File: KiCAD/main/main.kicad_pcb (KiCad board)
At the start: 2 copper layers, 46 parts, among them J1 USB_C_Receptacle_USB2.0_14P, J2 Conn_Coaxial, SW1 SW_SPDT, SW2 SW_Push, SW3 SW_Push, U1 SX1262IMLTRT, U2 TP4056-42-ESOP8, U3 TLV75533PDRV, U4 ESP32-S3-MINI-1, U5 BGS12WN6E6327, U7 CH340X

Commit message: rev 2!
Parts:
- removed D3, D4, D5: LED, LED_SMD:LED_0402_1005Metric
- removed R12: 1K, Resistor_SMD:R_01005_0402Metric
- removed R3, R8: 10K, Resistor_SMD:R_01005_0402Metric
- removed R6: 2K, Resistor_SMD:R_01005_0402Metric
- removed SW2: SW_Push, Button_Switch_SMD:SW_SPST_PTS810
- removed SW3: SW_Push, Button_Switch_SMD:SW_SPST_PTS645Sx43SMTR92
- removed U5: BGS12WN6E6327, Package_LGA:Infineon_PG-TSNP-6-10_0.7x1.1mm_0.7x1.1mm_P0.4mm
- added C5: 470pF, Capacitor_SMD:C_0603_1608Metric, F.Cu at (101.4, 78.9)
- added R10: 10K, Resistor_SMD:R_0603_1608Metric, F.Cu at (93.1, 48.9)
- added R9: 10K, Resistor_SMD:R_0603_1608Metric, F.Cu at (93.1, 45.4)
- added U6: MIC5219-3.3YMM, Package_SO:MSOP-8_3x3mm_P0.65mm, F.Cu at (97.2, 77.7)
- C1, C12, C14, C15, C16, C2: footprint Capacitor_SMD:C_01005_0402Metric -> Capacitor_SMD:C_0603_1608Metric
- C10, C11, C13, C17, C18, C3, C6, C7: footprint Capacitor_SMD:C_01005_0402Metric -> Capacitor_SMD:C_0402_1005Metric
- C4: footprint Capacitor_SMD:C_01005_0402Metric -> Capacitor_SMD:C_0805_2012Metric
- D1, D2: footprint Diode_SMD:D_01005_0402Metric -> Diode_SMD:D_SOD-323
- FL1: value 0900FM15K0039001E -> 0900FM15K0039; footprint customlib:0900FM15K0039001E_JOT-L -> RF_Converter:Balun_Johanson_0900FM15K0039
- G***: moved to B.Cu
- L1: footprint Inductor_SMD:L_01005_0402Metric -> Inductor_SMD:L_0805_2012Metric
- L2: footprint Inductor_SMD:L_01005_0402Metric -> Inductor_SMD:L_0603_1608Metric
- R1, R2, R4, R7: footprint Resistor_SMD:R_01005_0402Metric -> Resistor_SMD:R_0603_1608Metric
- R5: footprint Resistor_SMD:R_01005_0402Metric -> Resistor_SMD:R_0402_1005Metric
- SW1: footprint Button_Switch_SMD:SW_SPDT_PCM12 -> customlib:SSSS810701
- U3: value TLV75533PDRV -> BGS12P2L; footprint Package_SON:WSON-6-1EP_2x2mm_P0.65mm_EP1x1.6mm -> Package_LGA:Infineon_PG-TSNP-6-10_0.7x1.1mm_0.7x1.1mm_P0.4mm
- moved J2 142.7 mm to (100.3, 32.9), turned to 90 degrees
- moved G*** 100.0 mm to (105.5, 87.0), turned to 180 degrees
- moved C14 92.1 mm to (99.2, 40.1), turned to -135 degrees
- moved R4 67.2 mm to (97.1, 49.6), turned to 0 degrees
- moved C10 66.7 mm to (94.6, 47.5)
- moved C7 65.5 mm to (94.6, 45.0), turned to 90 degrees
- moved C1 63.1 mm to (94.8, 81.8)
- moved U1 62.6 mm to (98.8, 46.0), turned to -90 degrees
- moved D1 62.2 mm to (97.5, 84.0), turned to -90 degrees
- moved C11 62.0 mm to (95.6, 42.9), turned to 90 degrees
- moved L1 61.7 mm to (95.7, 41.0), turned to 180 degrees
- moved C16 61.2 mm to (91.8, 75.8)
- moved SW1 60.9 mm to (91.7, 82.5), turned to -90 degrees
- moved C15 60.9 mm to (101.0, 84.9), turned to 0 degrees
- moved C6 60.4 mm to (97.2, 42.4), turned to 180 degrees
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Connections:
- net CHRG renamed CHRG_BAT
- C13 pad 1: Net-(U5-CTRL) -> Net-(U3-CTRL)
- J1 pad A8: (no net) -> USB_DATA-
- R5 pad 2: Net-(U5-CTRL) -> Net-(U3-CTRL)
- U2 pad 6: Net-(D3-K) -> ~{STDBY}
- U2 pad 7: Net-(D4-K) -> ~{CHRG}
- U3 pad 1: VCC -> Net-(FL1-SW_RFO)
- U3 pad 2: unconnected-(U3-NC-Pad2) -> V-
- U3 pad 3: V- -> Net-(FL1-SW_RFI)
- U3 pad 4: Net-(SW1-A) -> VCC
- U3 pad 5: unconnected-(U3-NC-Pad5) -> Net-(J2-In)
- U3 pad 6: Net-(SW1-A) -> Net-(U3-CTRL)
- U4 pad 10: SPI_CLK -> SPI_MOSI
- U4 pad 11: SPI_MOSI -> READY
- U4 pad 12: SPI_MISO -> unconnected-(U4-IO8-Pad12)
- U4 pad 13: READY -> unconnected-(U4-IO9-Pad13)
- U4 pad 14: Net-(U4-IO10) -> unconnected-(U4-IO10-Pad14)
- U4 pad 20: unconnected-(U4-IO16-Pad20) -> ~{CHRG}
- U4 pad 21: unconnected-(U4-IO17-Pad21) -> ~{STDBY}
- U4 pad 29: unconnected-(U4-IO34-Pad29) -> IO34
- U4 pad 31: Net-(U4-IO35) -> IO35
- U4 pad 32: Net-(D5-K) -> IO36
- U4 pad 45: Net-(U4-EN) -> unconnected-(U4-EN-Pad45)
- U4 pad 7: unconnected-(U4-IO3-Pad7) -> SPI_CS
- U4 pad 8: unconnected-(U4-IO4-Pad8) -> SPI_CLK
- U4 pad 9: SPI_CS -> SPI_MISO
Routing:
- net V-: track 178.9 -> 259.0 mm, vias 9 -> 15
- net VCC: track 51.1 -> 108.9 mm, vias 2 -> 4
- net ~{STDBY}: track 0.00 -> 34.4 mm, vias 0 -> 2
- net ~{CHRG}: track 0.00 -> 28.7 mm, vias 0 -> 2
- net CHRG_BAT: track 4.51 -> 31.6 mm
- net V+: track 35.4 -> 50.0 mm, vias 0 -> 4
- net SERIAL_P: track 0.00 -> 13.5 mm, vias 0 -> 2
- net SERIAL_N: track 0.00 -> 13.5 mm, vias 0 -> 2
- net Net-(J2-In): track 0.00 -> 11.4 mm
- net Net-(U3-CTRL): track 0.00 -> 4.78 mm
- net SPI_CS: track 0.00 -> 4.62 mm
- net Net-(U2-PROG): track 1.96 -> 6.04 mm
- net Net-(D1-K): track 18.5 -> 14.5 mm
- net SPI_MOSI: track 0.00 -> 3.95 mm
- net SPI_CLK: track 0.00 -> 3.87 mm
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- added copper zone on F.Cu, net V-
- removed copper zone on B.Cu, net V-
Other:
- board outline added: 19.6 x 63.9 mm

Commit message: Rev2!
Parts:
- removed the G*** at (105.5, 87.0)
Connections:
- J1 pad A8: USB_DATA- -> (no net)
- SW1 pad 4.1: V- -> (no net)
- SW1 pad 4.2: V- -> (no net)
- SW1 pad 4.3: V- -> (no net)
- SW1 pad 4.4: V- -> (no net)
- U4 pad 29: IO34 -> unconnected-(U4-IO34-Pad29)
- U4 pad 31: IO35 -> unconnected-(U4-IO35-Pad31)
- U4 pad 32: IO36 -> unconnected-(U4-IO36-Pad32)
- U4 pad 35: unconnected-(U4-IO39-Pad35) -> TDI
- U4 pad 36: unconnected-(U4-IO40-Pad36) -> TDO
- U4 pad 37: unconnected-(U4-IO41-Pad37) -> TCK
- U4 pad 38: unconnected-(U4-IO42-Pad38) -> TMS

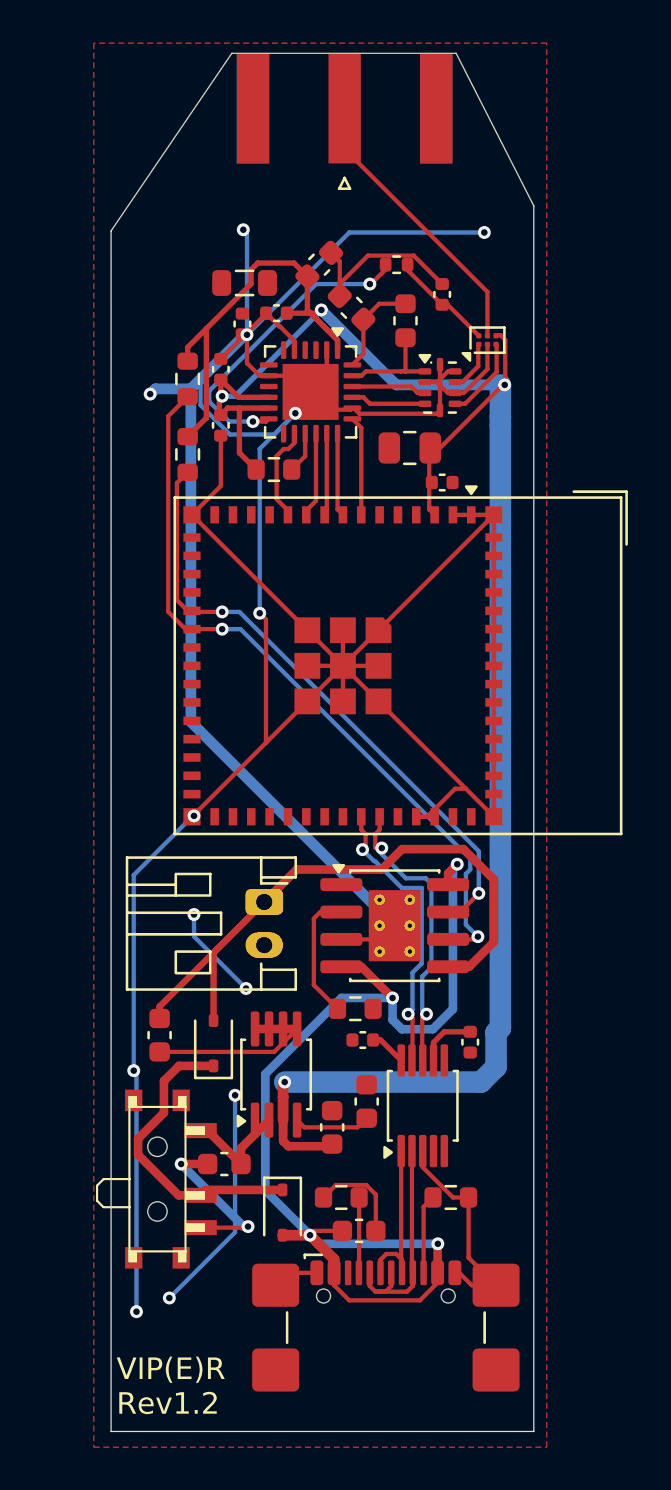
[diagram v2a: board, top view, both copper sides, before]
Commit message: added screen to rev 2 and bumped version to 2.1
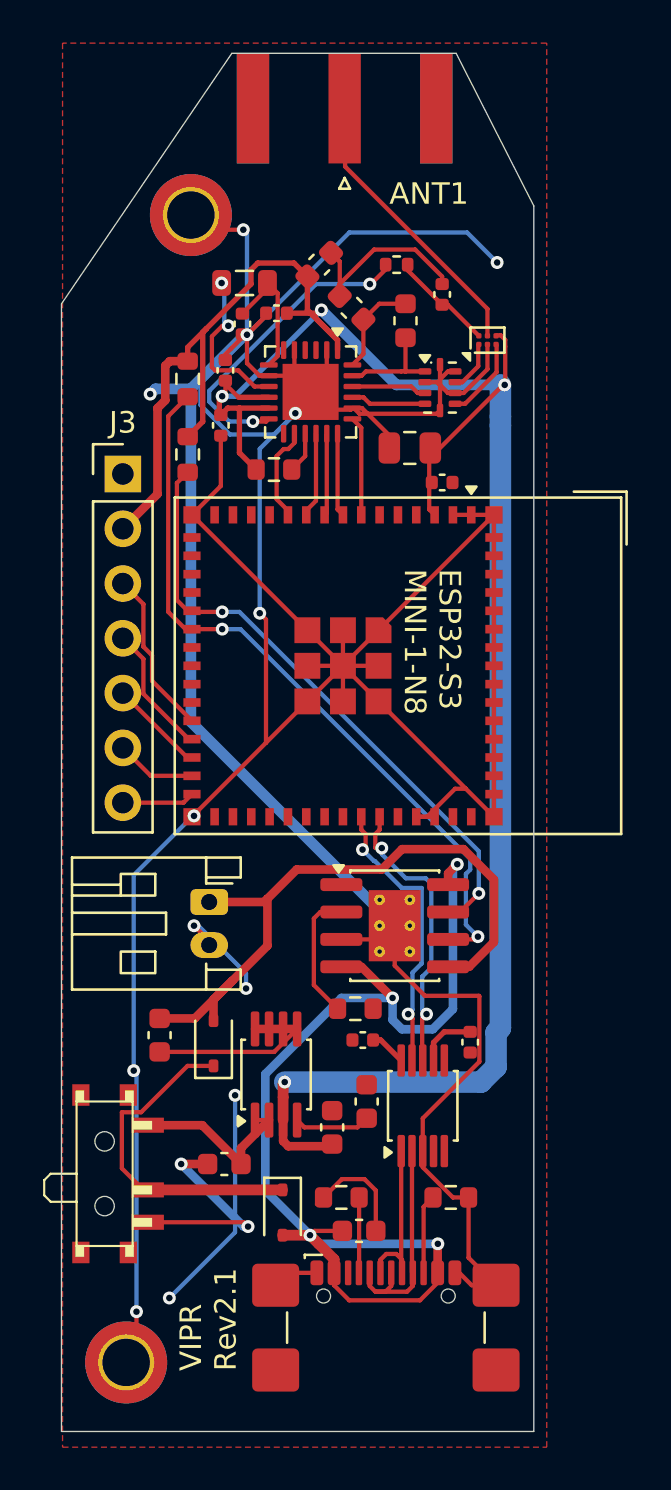
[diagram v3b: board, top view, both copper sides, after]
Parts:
- added H1: MountingHole_Pad, MountingHole:MountingHole_2.2mm_M2_DIN965_Pad_TopBottom, F.Cu at (90.2, 91.0)
- added H2: MountingHole_Pad, MountingHole:MountingHole_2.2mm_M2_DIN965_Pad_TopBottom, F.Cu at (93.2, 37.8)
- added J3: Conn_01x07_Socket, Connector_PinHeader_2.54mm:PinHeader_1x07_P2.54mm_Vertical, F.Cu at (90.0, 49.8)
- moved BT1 2.55 mm to (94.0, 69.7)
- moved SW1 2.46 mm to (89.2, 82.2)
- moved C7 0.22 mm to (94.8, 45.0)
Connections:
- U4 pad 26: unconnected-(U4-IO26-Pad26) -> SCR_CLK
- U4 pad 27: unconnected-(U4-IO47-Pad27) -> SCR_MOSI
- U4 pad 28: unconnected-(U4-IO33-Pad28) -> SCR_RES
- U4 pad 29: unconnected-(U4-IO34-Pad29) -> SCR_DC
- U4 pad 30: unconnected-(U4-IO48-Pad30) -> SCR_CS
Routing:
- net V-: track 259.0 -> 286.2 mm
- net VCC: track 108.9 -> 118.4 mm
- net SCR_CLK: track 0.00 -> 7.69 mm
- net Net-(U1-DCC_SW): track 0.00 -> 7.56 mm, vias 0 -> 2
- net SCR_MOSI: track 0.00 -> 6.09 mm
- net Net-(U1-VREG): track 0.00 -> 6.07 mm
- net SCR_RES: track 0.00 -> 4.44 mm
- net SCR_DC: track 0.00 -> 3.74 mm
- net Net-(SW1-A): track 5.09 -> 8.50 mm
- net SCR_CS: track 0.00 -> 3.37 mm
- net Net-(D1-K): track 14.5 -> 15.6 mm
- net CHRG_BAT: track 31.6 -> 30.7 mm
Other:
- board size 19.6 x 63.9 mm -> 21.9 x 63.9 mm
- board text added: "ANT1"
- board text added: "ESP32-S3 MINI-1-N8"
- board text added: "VIP(E)R Rev2.1"
- board text added: "VIPR Rev2.1"
- board text removed: "VIP(E)R Rev1.2"
